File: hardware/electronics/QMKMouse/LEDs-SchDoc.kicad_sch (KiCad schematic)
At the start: 20 parts

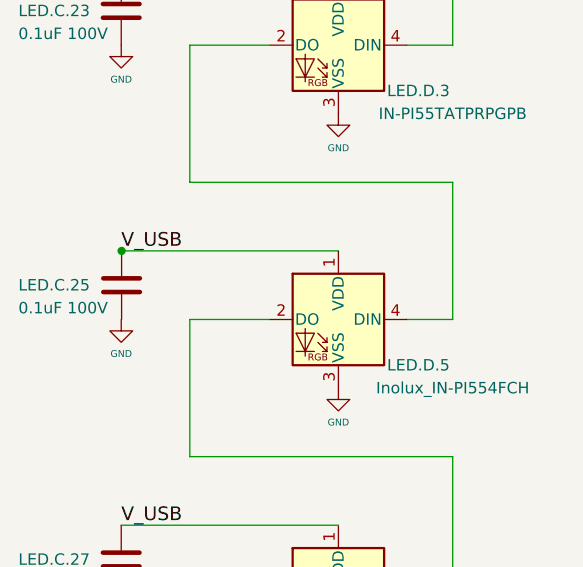
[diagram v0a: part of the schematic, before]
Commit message: fix ground connection of LED
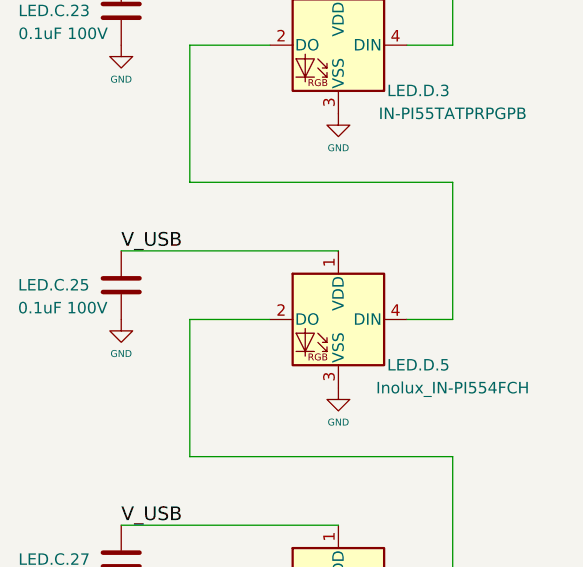
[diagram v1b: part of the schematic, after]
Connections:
- net GND: now also LED.C.25.1
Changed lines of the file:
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@@
   (junction (at 76.2 43.18) (diameter 0) (color 0 0 0 0)
-  )
-  (junction (at 66.0801 104.14) (diameter 0) (color 0 0 0 0)
   )
   (no_connect (at 205.74 157.48))
@@
     (stroke (width 0) (type default) (color 0 0 0 0))
   )
-  (wire (pts (xy 66.0801 104.14) (xy 90.17 104.14))
+  (wire (pts (xy 66.04 104.14) (xy 90.17 104.14))
     (stroke (width 0) (type default) (color 0 0 0 0))
   )
@@
   )
   (wire (pts (xy 234.95 96.52) (xy 234.95 111.76))
-    (stroke (width 0) (type default) (color 0 0 0 0))
-  )
-  (wire (pts (xy 66.04 104.14) (xy 66.0801 104.14))
     (stroke (width 0) (type default) (color 0 0 0 0))
   )
@@
     (pin "4")
   )
-  (symbol (lib_id "Device:C") (at 66.0801 107.95 0) (mirror x) (unit 1)
-    (in_bom yes) (on_board yes)
-    (property "Reference" "LED.C.25" (id 0) (at 54.61 107.95 0)
-      (effects (font (size 1.27 1.27)) (justify left))
-    )
-    (property "Value" "0.1uF 100V" (id 1) (at 54.61 110.49 0)
-      (effects (font (size 1.27 1.27)) (justify left))
-    )
-    (property "Footprint" "Chip_Passives.PcbLib:0805" (id 2) (at 67.0453 104.14 0)
-      (effects (font (size 1.27 1.27)) hide)
-    )
-    (property "Datasheet" "~" (id 3) (at 66.0801 107.95 0)
-      (effects (font (size 1.27 1.27)) hide)
-    )
+  (symbol (lib_id "Device:C") (at 66.04 107.95 0) (mirror x) (unit 1)
+    (in_bom yes) (on_board yes)
+    (property "Reference" "LED.C.25" (id 0) (at 54.5699 107.95 0)
+      (effects (font (size 1.27 1.27)) (justify left))
+    )
+    (property "Value" "0.1uF 100V" (id 1) (at 54.5699 110.49 0)
+      (effects (font (size 1.27 1.27)) (justify left))
+    )
+    (property "Footprint" "Chip_Passives.PcbLib:0805" (id 2) (at 67.0052 104.14 0)
+      (effects (font (size 1.27 1.27)) hide)
+    )
+    (property "Datasheet" "~" (id 3) (at 66.04 107.95 0)
+      (effects (font (size 1.27 1.27)) hide)
+    )

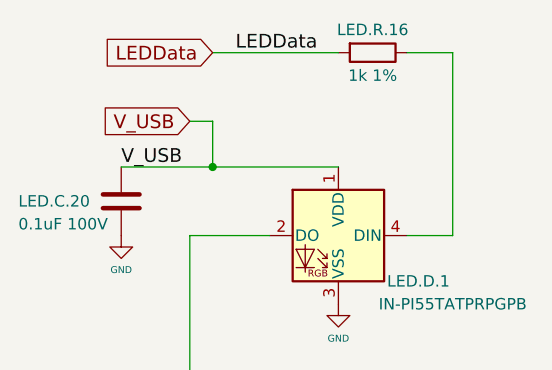
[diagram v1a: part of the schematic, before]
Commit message: fix ERC errors and use hierarchy labels
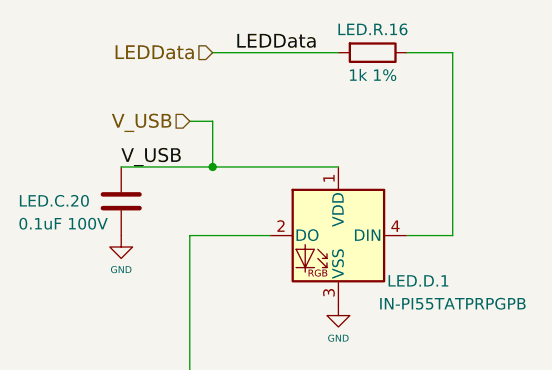
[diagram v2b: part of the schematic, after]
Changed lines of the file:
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@@
+    (stroke (width 0) (type default) (color 0 0 0 0))
+  )
+  (wire (pts (xy 234.95 81.28) (xy 229.87 81.28))
+    (stroke (width 0) (type default) (color 0 0 0 0))
+  )
+  (wire (pts (xy 73.66 142.24) (xy 73.66 147.32))
+    (stroke (width 0) (type default) (color 0 0 0 0))
+  )
+  (wire (pts (xy 205.74 81.28) (xy 214.63 81.28))
+    (stroke (width 0) (type default) (color 0 0 0 0))
+  )
+  (wire (pts (xy 73.66 111.76) (xy 82.55 111.76))
+    (stroke (width 0) (type default) (color 0 0 0 0))
+  )
+  (wire (pts (xy 234.95 111.76) (xy 229.87 111.76))
+    (stroke (width 0) (type default) (color 0 0 0 0))
+  )
+  (wire (pts (xy 73.66 96.52) (xy 102.87 96.52))
+    (stroke (width 0) (type default) (color 0 0 0 0))
+  )
+  (wire (pts (xy 205.74 157.48) (xy 205.74 154.94))
+    (stroke (width 0) (type default) (color 0 0 0 0))
+  )
+  (wire (pts (xy 73.66 66.04) (xy 102.87 66.04))
+    (stroke (width 0) (type default) (color 0 0 0 0))
+  )
+  (wire (pts (xy 102.87 30.48) (xy 102.87 50.8))
+    (stroke (width 0) (type default) (color 0 0 0 0))
+  )
+  (wire (pts (xy 66.04 73.66) (xy 90.17 73.66))
+    (stroke (width 0) (type default) (color 0 0 0 0))
+  )
+  (wire (pts (xy 198.12 134.62) (xy 222.25 134.62))
+    (stroke (width 0) (type default) (color 0 0 0 0))
+  )
+  (wire (pts (xy 66.04 104.14) (xy 90.17 104.14))
+    (stroke (width 0) (type default) (color 0 0 0 0))
+  )
+  (wire (pts (xy 205.74 111.76) (xy 205.74 127))
     (stroke (width 0) (type default) (color 0 0 0 0))
   )
   (wire (pts (xy 76.2 43.18) (xy 90.17 43.18))
-    (stroke (width 0) (type default) (color 0 0 0 0))
-  )
-  (wire (pts (xy 234.95 81.28) (xy 229.87 81.28))
-    (stroke (width 0) (type default) (color 0 0 0 0))
-  )
-  (wire (pts (xy 73.66 142.24) (xy 73.66 147.32))
-    (stroke (width 0) (type default) (color 0 0 0 0))
-  )
-  (wire (pts (xy 205.74 81.28) (xy 214.63 81.28))
-    (stroke (width 0) (type default) (color 0 0 0 0))
-  )
-  (wire (pts (xy 73.66 111.76) (xy 82.55 111.76))
-    (stroke (width 0) (type default) (color 0 0 0 0))
-  )
-  (wire (pts (xy 234.95 111.76) (xy 229.87 111.76))
-    (stroke (width 0) (type default) (color 0 0 0 0))
-  )
-  (wire (pts (xy 66.04 73.66) (xy 90.17 73.66))
-    (stroke (width 0) (type default) (color 0 0 0 0))
-  )
-  (wire (pts (xy 73.66 96.52) (xy 102.87 96.52))
-    (stroke (width 0) (type default) (color 0 0 0 0))
-  )
-  (wire (pts (xy 205.74 157.48) (xy 205.74 154.94))
-    (stroke (width 0) (type default) (color 0 0 0 0))
-  )
-  (wire (pts (xy 73.66 66.04) (xy 102.87 66.04))
-    (stroke (width 0) (type default) (color 0 0 0 0))
-  )
-  (wire (pts (xy 102.87 30.48) (xy 102.87 50.8))
-    (stroke (width 0) (type default) (color 0 0 0 0))
-  )
-  (wire (pts (xy 198.12 134.62) (xy 222.25 134.62))
-    (stroke (width 0) (type default) (color 0 0 0 0))
-  )
-  (wire (pts (xy 66.04 104.14) (xy 90.17 104.14))
-    (stroke (width 0) (type default) (color 0 0 0 0))
-  )
-  (wire (pts (xy 205.74 111.76) (xy 205.74 127))
     (stroke (width 0) (type default) (color 0 0 0 0))
   )
@@
     (effects (font (size 1.524 1.524)) (justify left bottom))
   )
-  (global_label "V_USB" (shape input) (at 73.66 38.1 180) (fields_autoplaced)
+  (hierarchical_label "LEDData" (shape input) (at 76.2 30.48 180)
     (effects (font (size 1.524 1.524)) (justify right))
-    (property "Intersheet References" "${INTERSHEET_REFS}" (id 0) (at 121.92 -76.2 0)
-      (effects (font (size 1.27 1.27)) (justify left) hide)
-    )
-  )
-  (global_label "LEDData" (shape input) (at 76.2 30.48 180) (fields_autoplaced)
+  )
+  (hierarchical_label "V_USB" (shape input) (at 73.66 38.1 180)
     (effects (font (size 1.524 1.524)) (justify right))
-    (property "Intersheet References" "${INTERSHEET_REFS}" (id 0) (at 124.46 -76.2 0)
-      (effects (font (size 1.27 1.27)) (justify left) hide)
-    )
   )
   (symbol (lib_id "power:GND") (at 198.12 142.24 0) (unit 1)
@@
     (pin "1")
   )
-  (symbol (lib_id "Mouse_Parts:Inolux_IN-PI55TATPRPGPB") (at 90.17 81.28 0) (mirror y) (unit 1)
+  (symbol (lib_name "Inolux_IN-PI55TATPRPGPB_2") (lib_id "Mouse_Parts:Inolux_IN-PI55TATPRPGPB") (at 90.17 81.28 0) (mirror y) (unit 1)
     (in_bom yes) (on_board yes)
     (property "Reference" "LED.D.3" (id 0) (at 99.06 86.36 0))
@@
     (pin "4")
   )
-  (symbol (lib_id "Mouse_Parts:Inolux_IN-PI55TATPRPGPB") (at 90.17 50.8 0) (mirror y) (unit 1)
+  (symbol (lib_name "Inolux_IN-PI55TATPRPGPB_1") (lib_id "Mouse_Parts:Inolux_IN-PI55TATPRPGPB") (at 90.17 50.8 0) (mirror y) (unit 1)
     (in_bom yes) (on_board yes)
     (property "Reference" "LED.D.1" (id 0) (at 99.06 55.88 0))
@@
     (pin "2")
   )
-  (symbol (lib_id "Mouse_Parts:Inolux_IN-PI55TATPRPGPB") (at 90.17 111.76 0) (mirror y) (unit 1)
+  (symbol (lib_name "Inolux_IN-PI55TATPRPGPB_6") (lib_id "Mouse_Parts:Inolux_IN-PI55TATPRPGPB") (at 90.17 111.76 0) (mirror y) (unit 1)
     (in_bom yes) (on_board yes)
     (property "Reference" "LED.D.5" (id 0) (at 99.06 116.84 0))
@@
     (pin "2")
   )
-  (symbol (lib_id "Mouse_Parts:Inolux_IN-PI55TATPRPGPB") (at 222.25 111.76 0) (mirror y) (unit 1)
+  (symbol (lib_name "Inolux_IN-PI55TATPRPGPB_3") (lib_id "Mouse_Parts:Inolux_IN-PI55TATPRPGPB") (at 222.25 111.76 0) (mirror y) (unit 1)
     (in_bom yes) (on_board yes)
     (property "Reference" "LED.D.6" (id 0) (at 231.14 116.84 0))
@@
     (pin "1")
   )
-  (symbol (lib_id "Mouse_Parts:Inolux_IN-PI55TATPRPGPB") (at 222.25 142.24 0) (mirror y) (unit 1)
+  (symbol (lib_name "Inolux_IN-PI55TATPRPGPB_4") (lib_id "Mouse_Parts:Inolux_IN-PI55TATPRPGPB") (at 222.25 142.24 0) (mirror y) (unit 1)
     (in_bom yes) (on_board yes)
     (property "Reference" "LED.D.8" (id 0) (at 231.14 147.32 0))
@@
     (pin "4")
   )
-  (symbol (lib_id "Mouse_Parts:Inolux_IN-PI55TATPRPGPB") (at 90.17 142.24 0) (mirror y) (unit 1)
+  (symbol (lib_name "Inolux_IN-PI55TATPRPGPB_5") (lib_id "Mouse_Parts:Inolux_IN-PI55TATPRPGPB") (at 90.17 142.24 0) (mirror y) (unit 1)
     (in_bom yes) (on_board yes)
     (property "Reference" "LED.D.7" (id 0) (at 99.06 147.32 0))
@@
     (pin "1")
   )
-  (symbol (lib_id "Mouse_Parts:Inolux_IN-PI55TATPRPGPB") (at 222.25 81.28 0) (mirror y) (unit 1)
+  (symbol (lib_name "Inolux_IN-PI55TATPRPGPB_7") (lib_id "Mouse_Parts:Inolux_IN-PI55TATPRPGPB") (at 222.25 81.28 0) (mirror y) (unit 1)
     (in_bom yes) (on_board yes)
     (property "Reference" "LED.D.4" (id 0) (at 231.14 86.36 0))

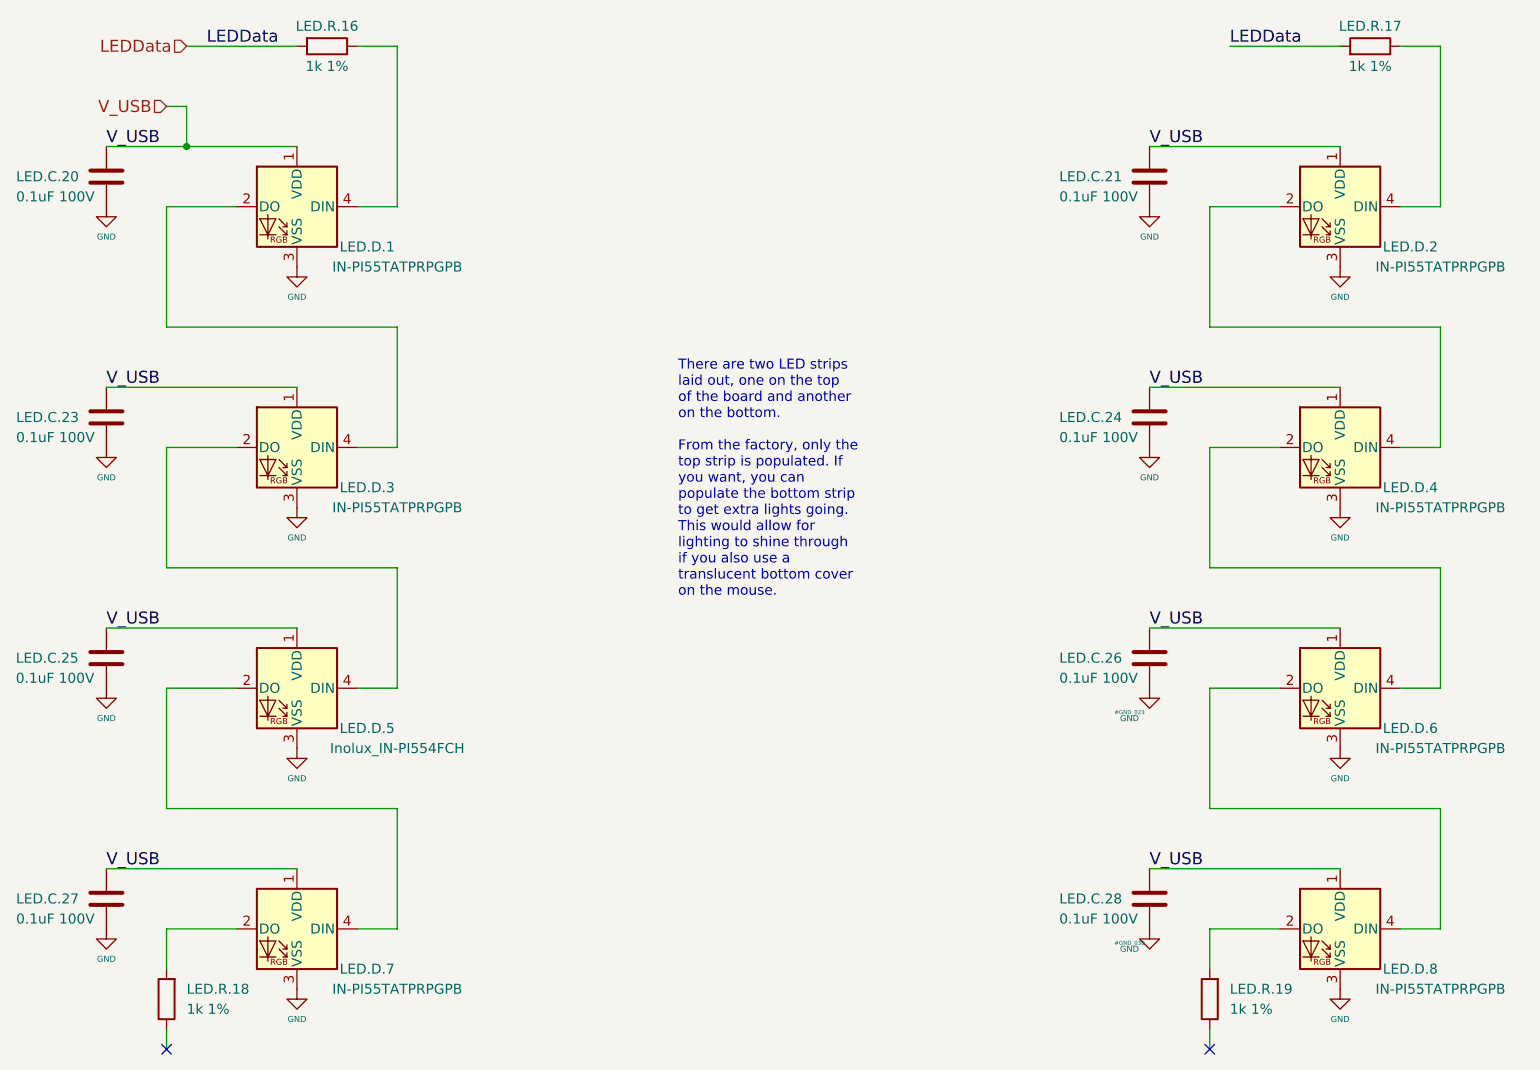
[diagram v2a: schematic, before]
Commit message: fix minor Schematic naming errors; improve BoM generation
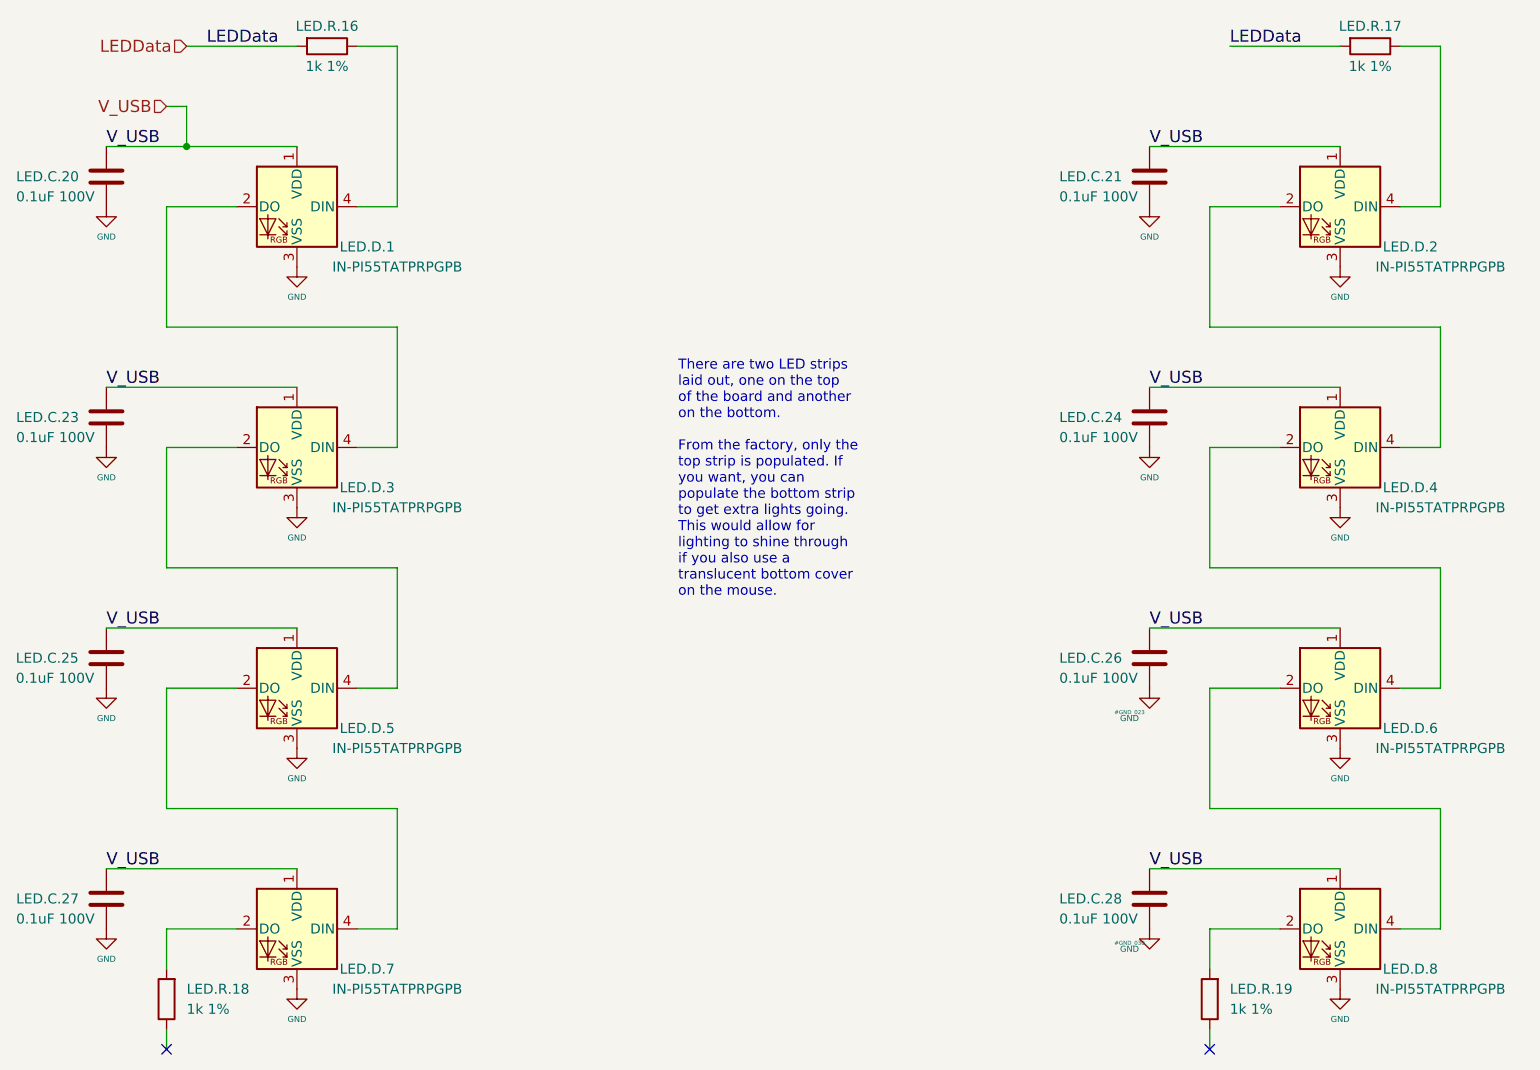
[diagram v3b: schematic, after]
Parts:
- LED.D.5: value Inolux_IN-PI554FCH -> IN-PI55TATPRPGPB
